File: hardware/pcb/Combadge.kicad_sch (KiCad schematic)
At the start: 20 parts, among them J1 Conn_01x02_Female, J3 TOUCH, J4 Conn_01x02_Female, U2 ESP32-WROOM-32, U4 MAX98357AEWL+T

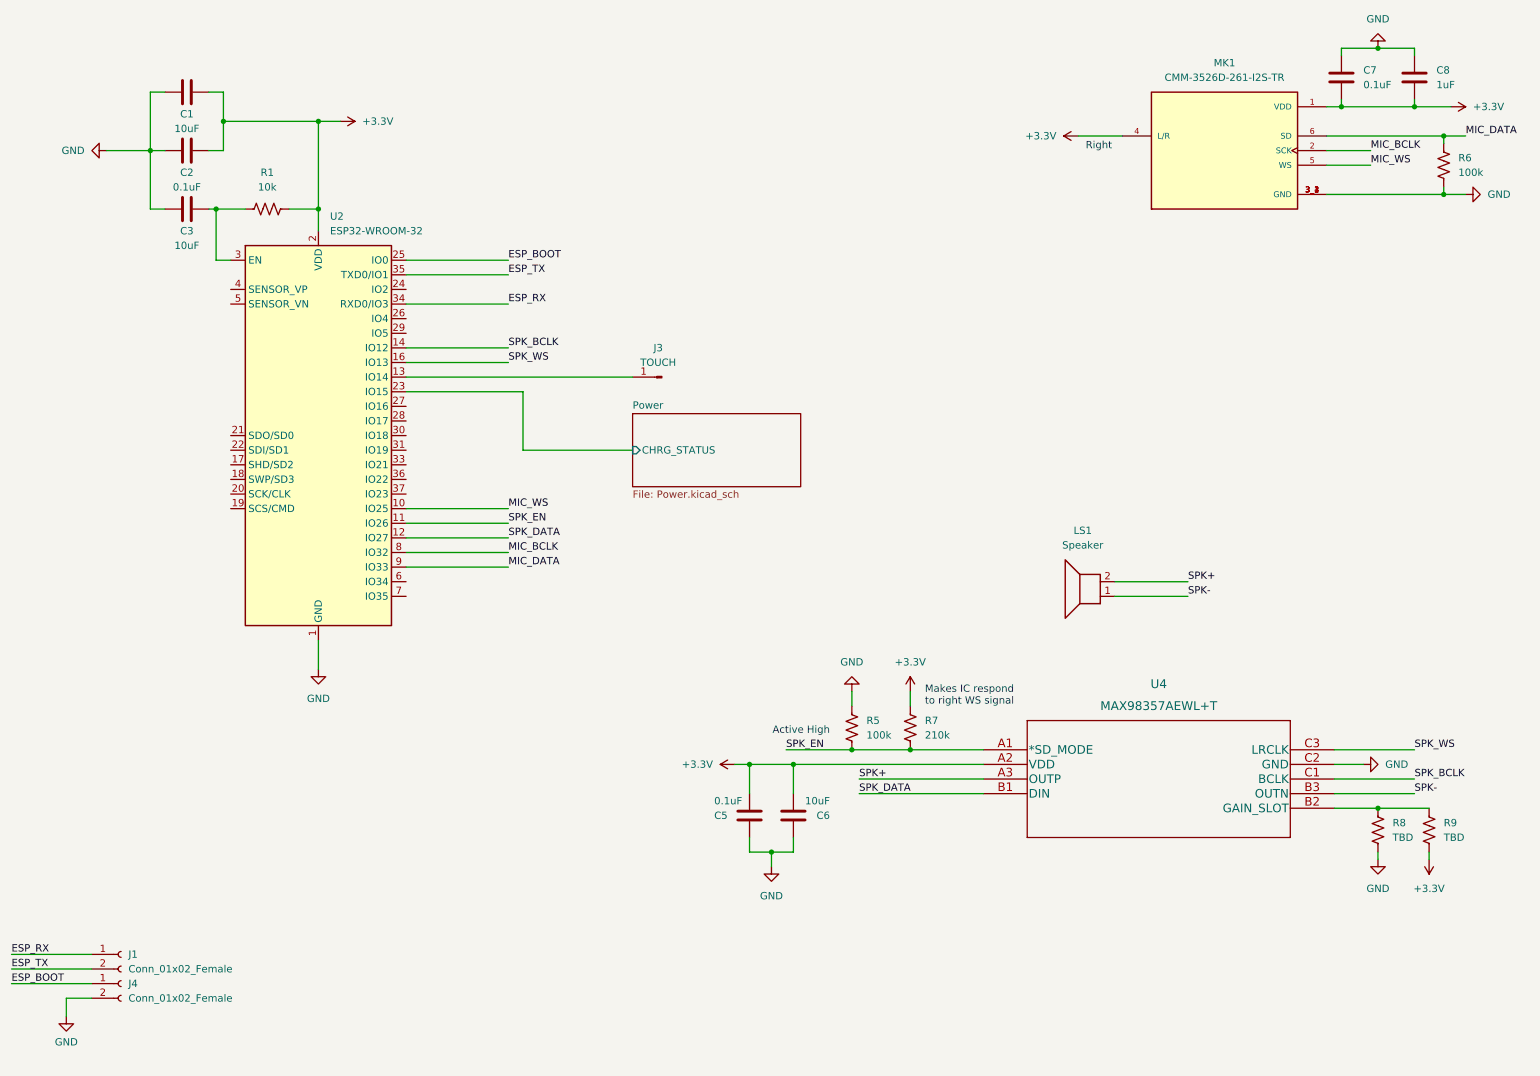
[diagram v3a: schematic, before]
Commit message: Replace XC6808 with MCP73831 in schematic
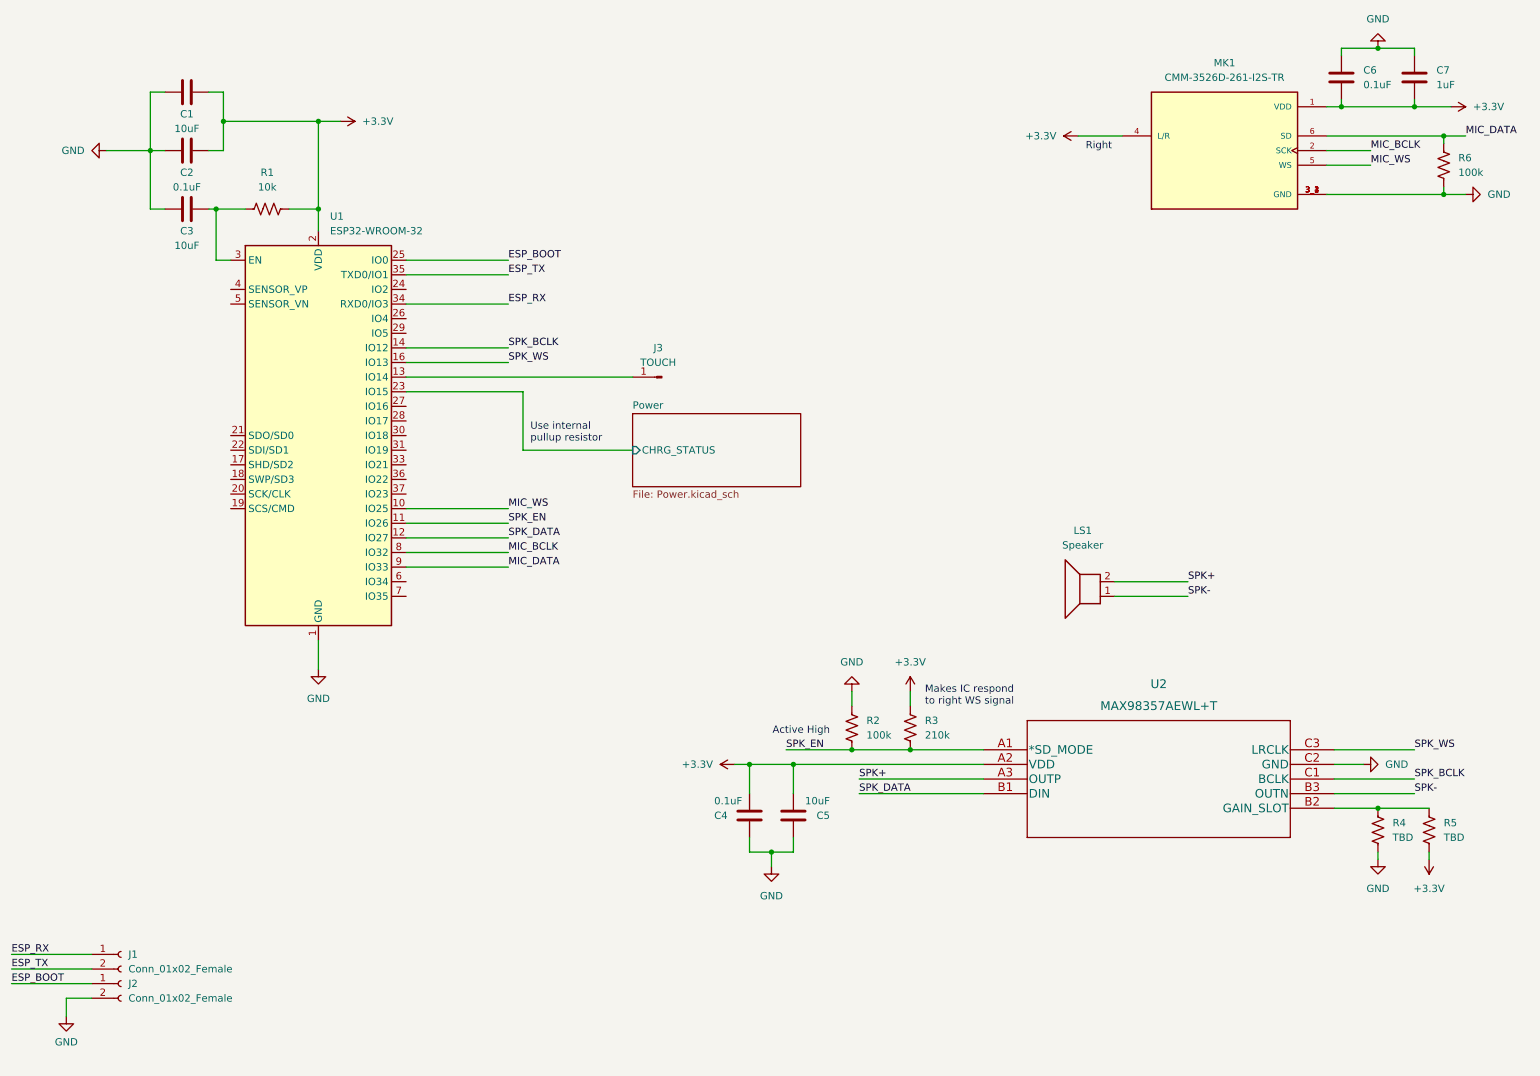
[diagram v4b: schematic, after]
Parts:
- renumbered C5 to C4, C6 to C5, C7 to C6, C8 to C7, J4 to J2, R5 to R2, R7 to R3, R8 to R4, R9 to R5, U2 to U1, U4 to U2
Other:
- note added: "Use internal pullup resistor"

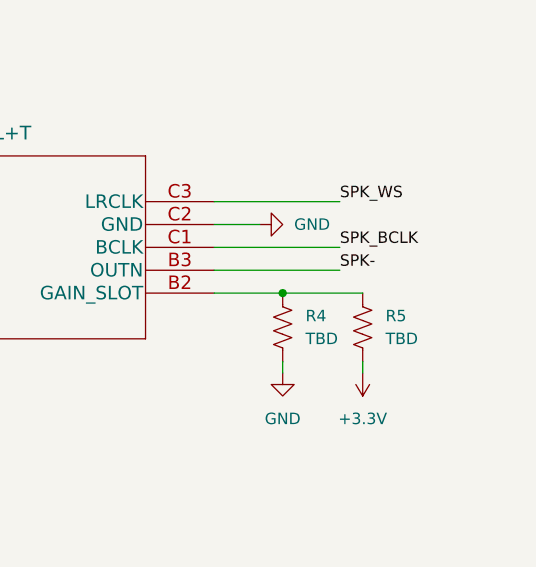
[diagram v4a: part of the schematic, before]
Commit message: Add MCP73831 to PCB
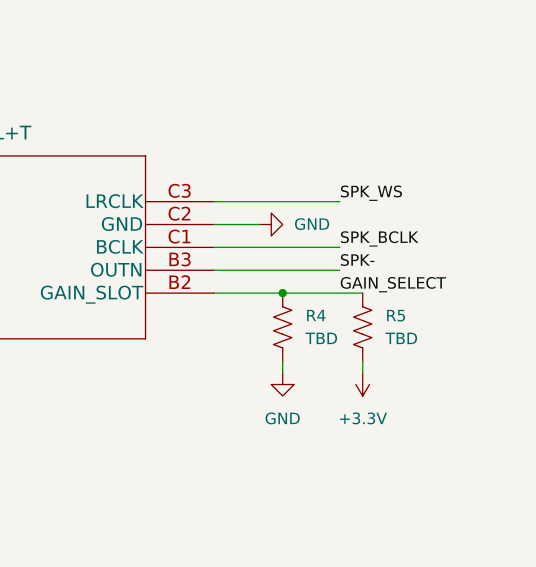
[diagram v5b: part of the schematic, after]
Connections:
- net GAIN_SELECT: now reaches R4.1, R5.1, U2.B2 (GAIN_SLOT)
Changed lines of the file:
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@@
+    (effects (font (size 1.27 1.27)) (justify left bottom))
+  )
+  (label "GAIN_SELECT" (at 264.16 151.13 0) (fields_autoplaced)
     (effects (font (size 1.27 1.27)) (justify left bottom))
   )

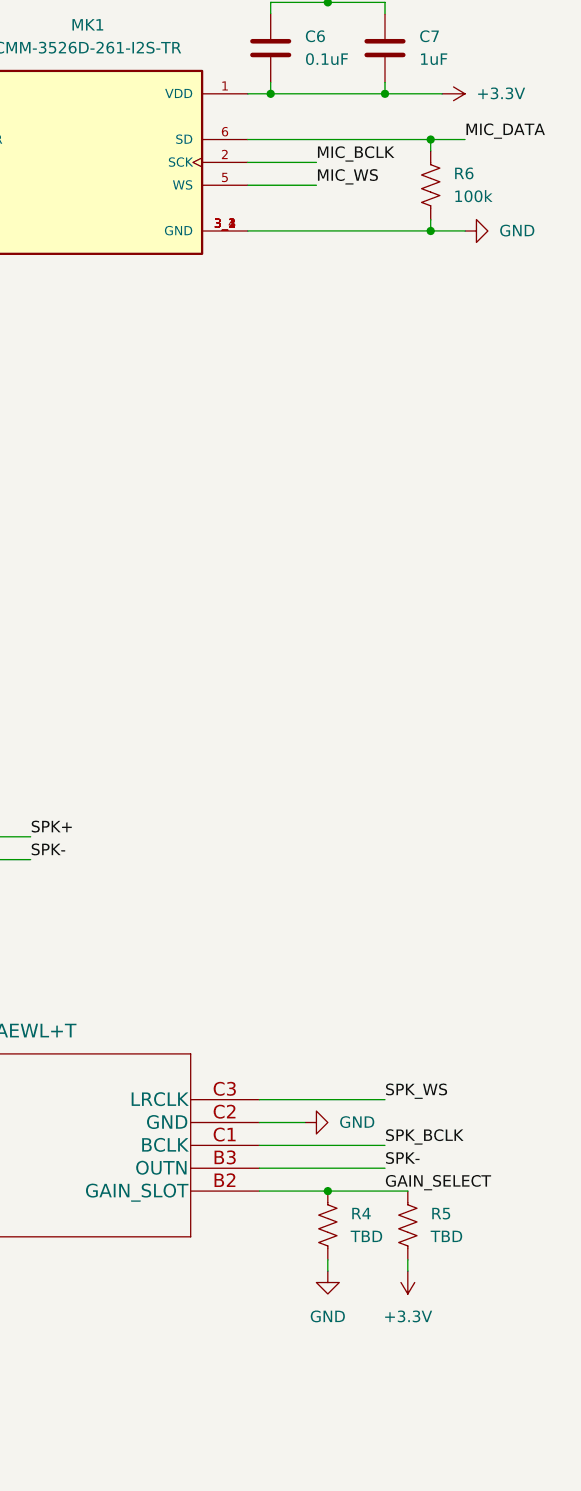
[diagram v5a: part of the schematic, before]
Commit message: Use single resistor for setting amplifier gain
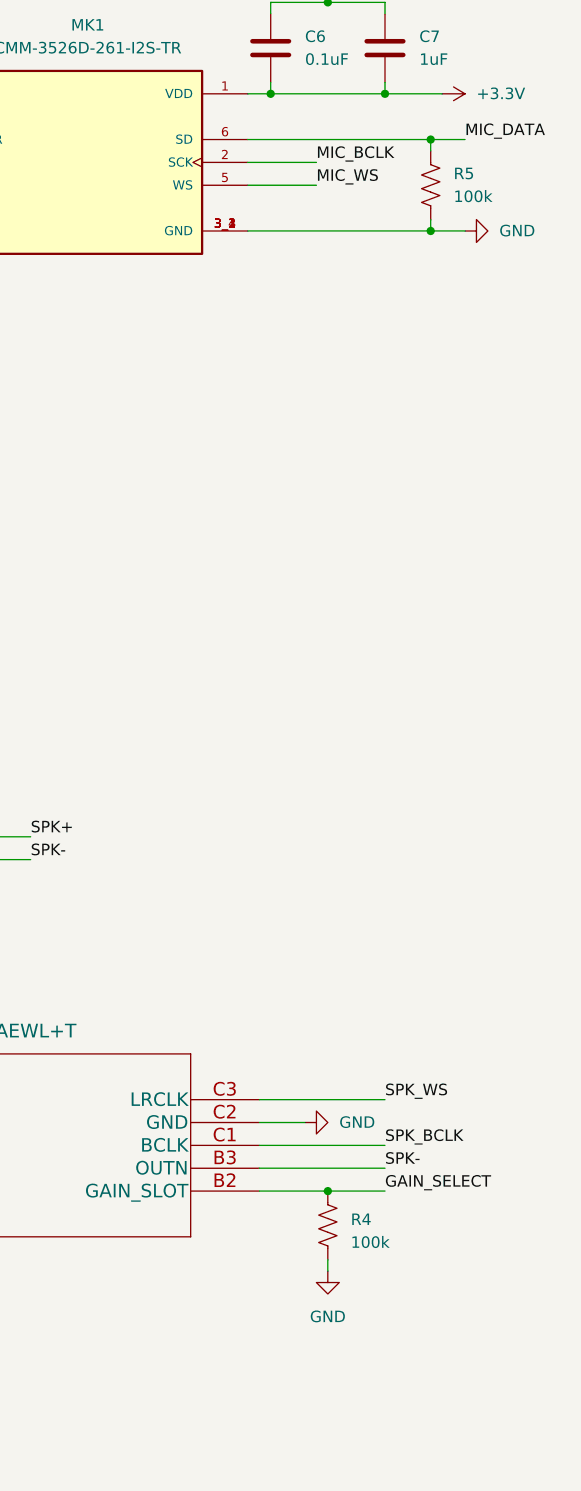
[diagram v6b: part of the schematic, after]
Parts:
- removed R5: TBD, Resistor_SMD:R_1206_3216Metric_Pad1.30x1.75mm_HandSolder, symbol Device:R_US
- R4: value TBD -> 100k
- renumbered R6 to R5
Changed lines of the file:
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@@
     (rev "1")
   )
+  (junction (at 257.81 151.13) (diameter 0) (color 0 0 0 0)
+  )
   (junction (at 257.81 19.05) (diameter 0) (color 0 0 0 0)
   )
@@
   (junction (at 148.59 143.51) (diameter 0) (color 0 0 0 0)
   )
-  (junction (at 257.81 151.13) (diameter 0) (color 0 0 0 0)
-  )
   (junction (at 73.66 31.75) (diameter 0) (color 0 0 0 0)
   )
@@
     (stroke (width 0) (type default))
   )
+  (wire (pts (xy 57.15 31.75) (xy 73.66 31.75))
+    (stroke (width 0) (type default))
+  )
+  (wire (pts (xy 44.45 26.67) (xy 44.45 36.83))
+    (stroke (width 0) (type default))
+  )
+  (wire (pts (xy 68.58 46.99) (xy 73.66 46.99))
+    (stroke (width 0) (type default))
+  )
+  (wire (pts (xy 250.19 146.05) (xy 264.16 146.05))
+    (stroke (width 0) (type default))
+  )
+  (wire (pts (xy 54.61 26.67) (xy 57.15 26.67))
+    (stroke (width 0) (type default))
+  )
   (wire (pts (xy 250.19 151.13) (xy 257.81 151.13))
     (stroke (width 0) (type default))
   )
-  (wire (pts (xy 57.15 31.75) (xy 73.66 31.75))
-    (stroke (width 0) (type default))
-  )
-  (wire (pts (xy 44.45 26.67) (xy 44.45 36.83))
-    (stroke (width 0) (type default))
-  )
-  (wire (pts (xy 68.58 46.99) (xy 73.66 46.99))
-    (stroke (width 0) (type default))
-  )
-  (wire (pts (xy 250.19 146.05) (xy 264.16 146.05))
-    (stroke (width 0) (type default))
-  )
-  (wire (pts (xy 54.61 26.67) (xy 57.15 26.67))
-    (stroke (width 0) (type default))
-  )
-  (wire (pts (xy 257.81 151.13) (xy 266.7 151.13))
-    (stroke (width 0) (type default))
-  )
   (wire (pts (xy 212.09 114.3) (xy 224.79 114.3))
     (stroke (width 0) (type default))
@@
     (stroke (width 0) (type default))
   )
-  (wire (pts (xy 266.7 158.75) (xy 266.7 160.02))
-    (stroke (width 0) (type default))
-  )
   (wire (pts (xy 148.59 143.51) (xy 156.21 143.51))
     (stroke (width 0) (type default))
@@
   )
   (wire (pts (xy 205.74 34.29) (xy 213.36 34.29))
+    (stroke (width 0) (type default))
+  )
+  (wire (pts (xy 257.81 151.13) (xy 264.16 151.13))
     (stroke (width 0) (type default))
   )
@@
   (label "SPK_DATA" (at 106.68 104.14 0) (fields_autoplaced)
     (effects (font (size 1.27 1.27)) (justify left bottom))
-  )
-  (symbol (lib_id "power:+3.3V") (at 266.7 160.02 180) (unit 1)
-    (in_bom yes) (on_board yes) (dnp no) (fields_autoplaced)
-    (property "Reference" "#PWR013" (at 266.7 156.21 0)
-      (effects (font (size 1.27 1.27)) hide)
-    )
-    (property "Value" "+3.3V" (at 266.7 165.1 0)
-      (effects (font (size 1.27 1.27)))
-    )
-    (property "Footprint" "" (at 266.7 160.02 0)
-      (effects (font (size 1.27 1.27)) hide)
-    )
-    (property "Datasheet" "" (at 266.7 160.02 0)
-      (effects (font (size 1.27 1.27)) hide)
-    )
-    (pin "1")
-    (instances
-      (project "Combadge"
-        (path "/dc42e7bc-f663-434d-8744-232038ac4fdf"
-          (reference "#PWR013") (unit 1)
-        )
-      )
-    )
   )
   (symbol (lib_id "power:+3.3V") (at 146.05 143.51 90) (unit 1)
@@
   (symbol (lib_id "Device:R_US") (at 257.81 154.94 0) (unit 1)
     (in_bom yes) (on_board yes) (dnp no) (fields_autoplaced)
-    (property "Reference" "R4" (at 260.35 153.6699 0)
-      (effects (font (size 1.27 1.27)) (justify left))
-    )
-    (property "Value" "TBD" (at 260.35 156.2099 0)
+    (property "Reference" "R4" (at 260.35 154.305 0)
+      (effects (font (size 1.27 1.27)) (justify left))
+    )
+    (property "Value" "100k" (at 260.35 156.845 0)
       (effects (font (size 1.27 1.27)) (justify left))
     )
@@
   (symbol (lib_id "power:+3.3V") (at 270.51 29.21 270) (unit 1)
     (in_bom yes) (on_board yes) (dnp no) (fields_autoplaced)
-    (property "Reference" "#PWR014" (at 266.7 29.21 0)
+    (property "Reference" "#PWR013" (at 266.7 29.21 0)
       (effects (font (size 1.27 1.27)) hide)
     )
@@
       (project "Combadge"
         (path "/dc42e7bc-f663-434d-8744-232038ac4fdf"
-          (reference "#PWR014") (unit 1)
+          (reference "#PWR013") (unit 1)
         )
       )
@@
   (symbol (lib_id "power:GND") (at 273.05 44.45 90) (unit 1)
     (in_bom yes) (on_board yes) (dnp no)
-    (property "Reference" "#PWR015" (at 279.4 44.45 0)
+    (property "Reference" "#PWR014" (at 279.4 44.45 0)
       (effects (font (size 1.27 1.27)) hide)
     )
@@
       (project "Combadge"
         (path "/dc42e7bc-f663-434d-8744-232038ac4fdf"
-          (reference "#PWR015") (unit 1)
+          (reference "#PWR014") (unit 1)
         )
       )
@@
   (symbol (lib_id "Device:R_US") (at 269.24 39.37 0) (unit 1)
     (in_bom yes) (on_board yes) (dnp no) (fields_autoplaced)
-    (property "Reference" "R6" (at 271.78 38.0999 0)
+    (property "Reference" "R5" (at 271.78 38.0999 0)
       (effects (font (size 1.27 1.27)) (justify left))
     )
@@
       (project "Combadge"
         (path "/dc42e7bc-f663-434d-8744-232038ac4fdf"
-          (reference "R6") (unit 1)
+          (reference "R5") (unit 1)
         )
       )
@@
         )
       )
-    )
-  )
-  (symbol (lib_id "Device:R_US") (at 266.7 154.94 0) (unit 1)
-    (in_bom yes) (on_board yes) (dnp no) (fields_autoplaced)
-    (property "Reference" "R5" (at 269.24 153.6699 0)
-      (effects (font (size 1.27 1.27)) (justify left))
-    )
-    (property "Value" "TBD" (at 269.24 156.2099 0)
-      (effects (font (size 1.27 1.27)) (justify left))
-    )
-    (property "Footprint" "Resistor_SMD:R_1206_3216Metric_Pad1.30x1.75mm_HandSolder" (at 267.716 155.194 90)
-      (effects (font (size 1.27 1.27)) hide)
-    )
-    (property "Datasheet" "~" (at 266.7 154.94 0)
-      (effects (font (size 1.27 1.27)) hide)
-    )
-    (pin "1")
-    (pin "2")
-    (instances
-      (project "Combadge"
-        (path "/dc42e7bc-f663-434d-8744-232038ac4fdf"
-          (reference "R5") (unit 1)
-        )
-      )
